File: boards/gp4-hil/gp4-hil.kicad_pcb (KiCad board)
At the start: 4 copper layers, 160 x 62 mm, 452 parts, among them J1 BEL_FUSE_0826-1G1T-23-F, J2 XILINX_JTAG, J3 XILINX_JTAG_ICESIDE, J4 XILINX_JTAG_ICESIDE, K1 CONN_3_PWROUT, P1 GPAK_ZIF, P2 2x10 HEADER, Q1 SSM6N58NU, Q11 SSM6N58NU, Q12 DMP2069UFY4, Q13 SSM6N58NU, Q14 SSM6N58NU, Q15 SSM6N58NU, Q16 SSM6N58NU, Q17 SSM6N58NU, Q18 SSM6N58NU, Q19 SSM6N58NU, Q20 SSM6N58NU, Q21 SSM6N58NU, Q22 DMP2069UFY4, U1 MIC2288-DFN, U10 AD9609, U11 DAC084S085, U12 DAC084S085, U13 DAC084S085, U14 DAC084S085, U15 TS3A4751, U16 TS3A4751, U17 TS3A4751, U18 TS3A4751, U19 TS3A4751, U2 XC7A100T-1FTG256C, U20 SIP32408, U21 SIP32408, U22 SIP32408, U23 SIP32408, U24 SIP32408, U25 TS3A4751, U26 TS3A4751, U27 TS3A4751, U28 TS3A4751, U29 TXB0104RUT, U3 LTC3374-QFN, U30 TXB0104RUT, U31 ADA4937-2, U32 SIP32408, U33 125 MHz, U34 INA199A2RSW, U35 INA199A2RSW, U36 INA199A2RSW, U4 SIP32408, U5 KSZ9031RN, U6 W25Q32FW, U7 25 MHz, U8 ADG726, U9 AD9609

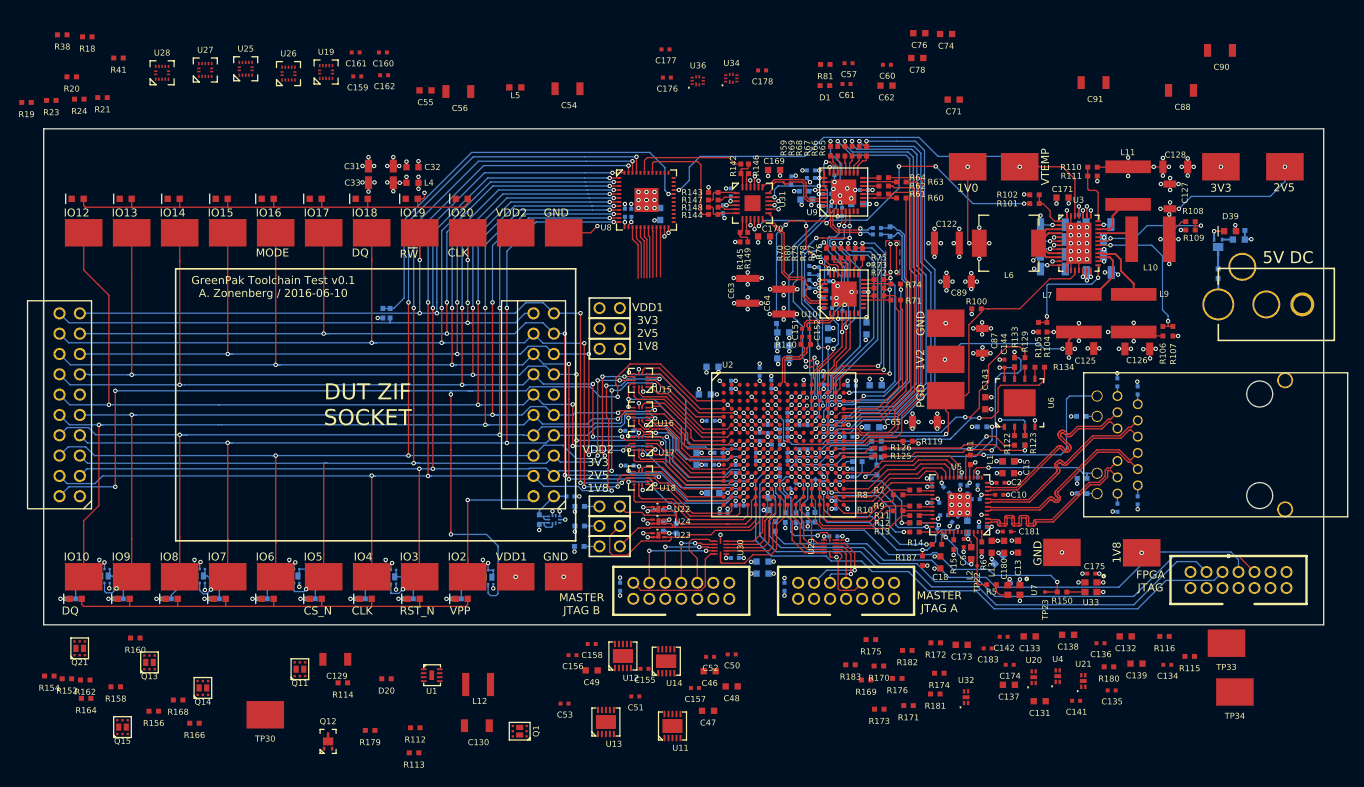
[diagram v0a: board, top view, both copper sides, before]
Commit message: Continued work on dev board layout. Hooked up analog mux.
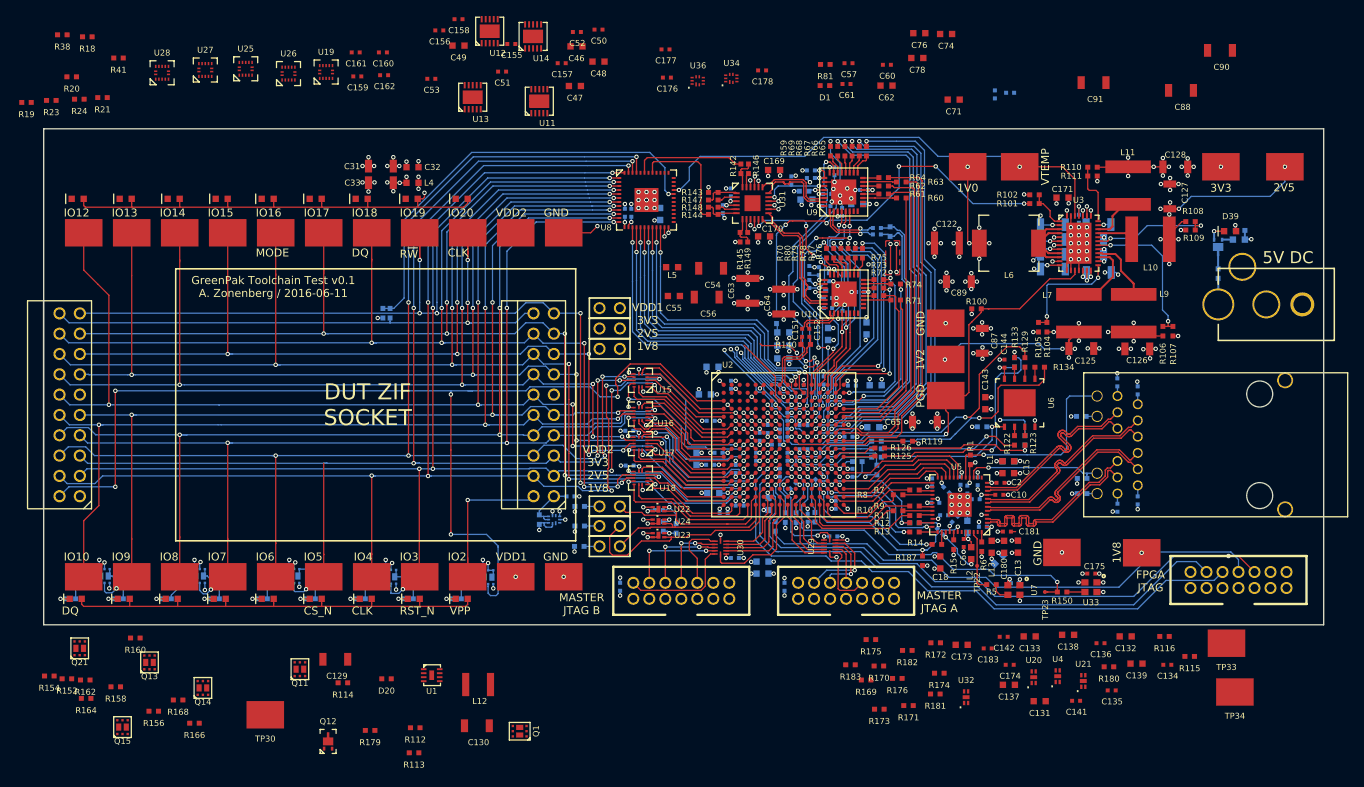
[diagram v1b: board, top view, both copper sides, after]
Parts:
- moved C157 79.9 mm to (85.8, 49.8)
- moved C158 79.9 mm to (72.8, 44.3)
- moved U11 79.9 mm to (83.0, 54.5)
- moved U12 79.9 mm to (76.8, 45.8)
- moved U13 79.9 mm to (74.6, 54.0)
- moved C155 79.9 mm to (79.5, 47.4)
- moved C156 79.9 mm to (70.5, 45.7)
- moved C46 79.9 mm to (87.6, 47.7)
- moved C47 79.9 mm to (87.4, 52.6)
- moved C48 79.9 mm to (90.3, 49.6)
- moved C49 79.9 mm to (72.8, 47.6)
- moved C50 79.9 mm to (90.3, 45.6)
- moved C51 79.9 mm to (78.3, 50.9)
- moved C52 79.9 mm to (87.7, 45.9)
- moved C53 79.9 mm to (69.5, 51.8)
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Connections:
- U2 pad A10: /Analog IO/MUX_WR_N -> /Analog IO/MUX_CS_B_N
- U2 pad B10: /Analog IO/MUX_EN_N -> /Analog IO/MUX_CS_A_N
- U2 pad B11: /Analog IO/MUX_A3 -> /Analog IO/MUX_WR_N
- U2 pad B9: /Analog IO/MUX_CS_B_N -> /Analog IO/MUX_A1
- U2 pad C11: /Analog IO/DAC_SYNC_N -> /Analog IO/MUX_EN_N
- U2 pad C8: /Analog IO/MUX_A1 -> /Analog IO/DAC_B_DIN
- U2 pad C9: /Analog IO/MUX_A2 -> /Analog IO/MUX_A0
- U2 pad D10: /Analog IO/MUX_A0 -> /Analog IO/MUX_A2
- U2 pad D11: /Analog IO/DAC_B_DIN -> /Analog IO/MUX_A3
- U2 pad G11: /Analog IO/MUX_CS_A_N -> /Analog IO/DAC_SYNC_N
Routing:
- net /Analog IO/MUX_A3: track 6.47 -> 39.7 mm, vias 0 -> 2
- net /Analog IO/MUX_EN_N: track 6.20 -> 37.8 mm, vias 0 -> 2
- net /Analog IO/MUX_A2: track 7.24 -> 38.8 mm, vias 1 -> 2
- net /Analog IO/MUX_A0: track 7.40 -> 38.0 mm, vias 1 -> 2
- net /Analog IO/MUX_WR_N: track 6.20 -> 36.5 mm, vias 0 -> 2
- net /Analog IO/MUX_CS_A_N: track 6.36 -> 35.9 mm, vias 0 -> 2
- net /Analog IO/MUX_A1: track 7.26 -> 35.9 mm, vias 1 -> 2
- net /Analog IO/MUX_CS_B_N: track 6.32 -> 35.0 mm, vias 0 -> 2
- net /Analog IO/DAC_SYNC_N: track 0.57 -> 17.9 mm, vias 1 -> 2
- net /Analog IO/DAC_A_DIN: track 0.71 -> 14.3 mm, vias 1 -> 2
- net /Analog IO/DAC_C_DIN: track 0.71 -> 10.2 mm, vias 1 -> 2
- net /Analog IO/DAC_SCLK: track 0.71 -> 9.98 mm, vias 1 -> 2
- net /Analog IO/DAC_B_DIN: track 0.57 -> 8.79 mm, vias 1 -> 0
- net /Analog IO/DAC_D_DIN: track 9.99 -> 17.3 mm, vias 3 -> 4
- net /Analog IO/DUT_VDD1: track 150.9 -> 149.1 mm
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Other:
- board text added: "GreenPak Toolchain Test v0.1 A. Zonenberg / 2016-06-11"
- board text removed: "GreenPak Toolchain Test v0.1 A. Zonenberg / 2016-06-10"

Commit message: Continued layout, down to 288 unrouted nets. Working mostly on ADC inputs plus bus re-routing.
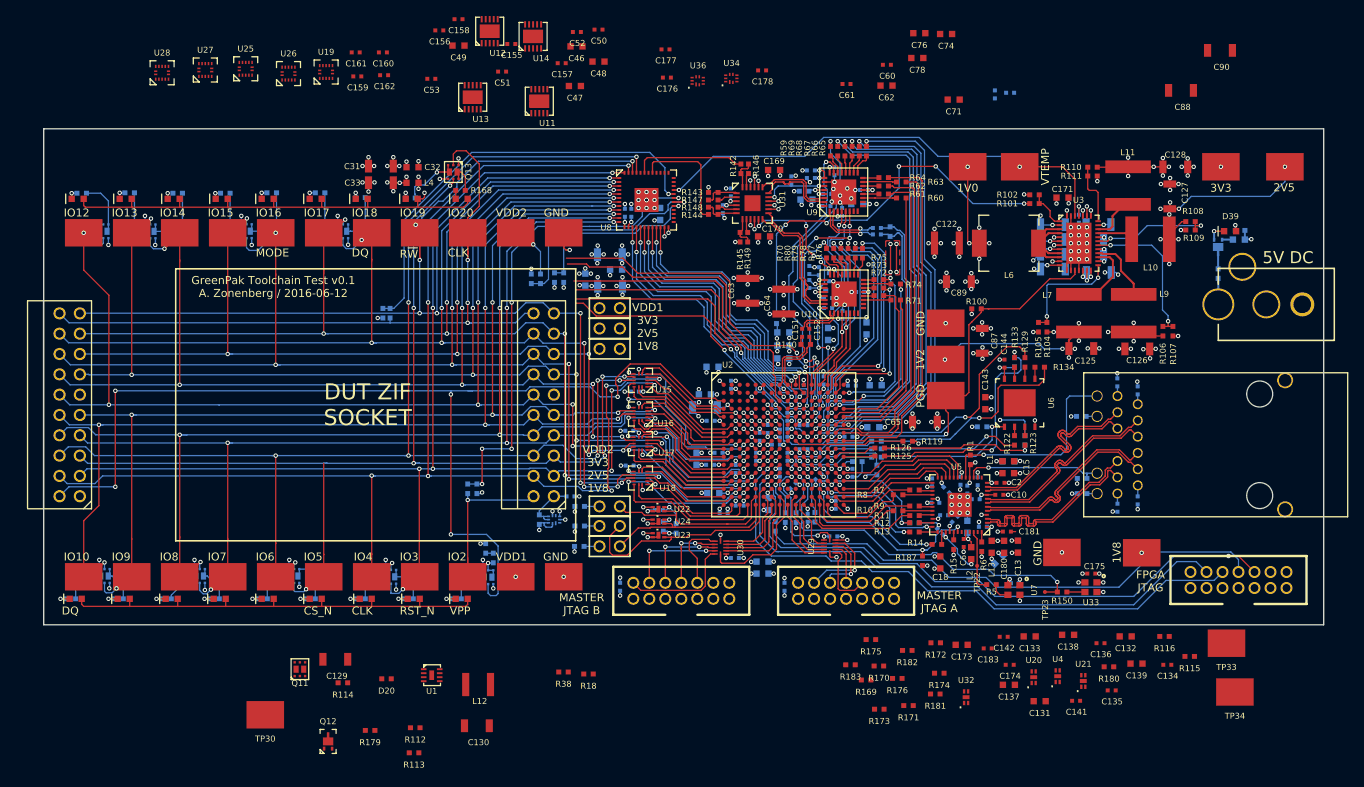
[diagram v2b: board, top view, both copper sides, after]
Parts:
- C54, C55, C56, C57, C91, D1, L5, Q1, Q14, Q15, Q21, R152, R154, R156, R158, R160, R162, R164, R166, R19, R20, R21, R23, R24, R41, R81: moved to B.Cu
- moved R18 101.3 mm to (89.1, 126.2)
- moved R38 101.3 mm to (86.0, 125.9)
- moved Q1 81.3 mm to (28.4, 70.8), turned to 180 degrees
- moved R81 74.4 mm to (77.2, 111.7), turned to 270 degrees
- moved R168 72.8 mm to (73.1, 65.7), turned to 180 degrees
- moved Q13 72.1 mm to (72.2, 63.4), turned to 180 degrees
- moved D1 71.7 mm to (76.2, 110.5), turned to 90 degrees
- moved R20 71.4 mm to (74.0, 103.0), turned to 270 degrees
- moved R164 71.4 mm to (60.6, 66.6), turned to 180 degrees
- moved R166 71.0 mm to (66.8, 66.7), turned to 180 degrees
- moved R41 70.0 mm to (75.2, 103.0), turned to 90 degrees
- moved R19 69.5 mm to (84.8, 76.6), turned to 270 degrees
- moved R23 67.8 mm to (86.0, 76.6), turned to 90 degrees
- moved R162 67.6 mm to (55.5, 66.0), turned to 180 degrees
- moved R156 64.8 mm to (37.7, 66.0), turned to 180 degrees
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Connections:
- Q1 pad G1: /Analog IO/DUT_GPIO18 -> /Analog IO/DUT_GPIO12
- Q11 pad D2: Net-(Q11-PadD2) -> (no net)
- Q11 pad G2: /Analog IO/DUT_GPIO19 -> (no net)
- Q11 pad S2: /Analog IO/GND -> (no net)
- Q13 pad G1: /Analog IO/DUT_GPIO15 -> /Analog IO/DUT_GPIO20
- Q13 pad G2: /Analog IO/DUT_GPIO12 -> /Analog IO/DUT_GPIO19
- Q14 pad G1: /Analog IO/DUT_GPIO16 -> /Analog IO/DUT_GPIO18
- Q14 pad G2: /Analog IO/DUT_GPIO13 -> /Analog IO/DUT_GPIO17
- Q15 pad G1: /Analog IO/DUT_GPIO17 -> /Analog IO/DUT_GPIO16
- Q15 pad G2: /Analog IO/DUT_GPIO14 -> /Analog IO/DUT_GPIO15
- Q21 pad D2: (no net) -> Net-(Q21-PadD2)
- Q21 pad G1: /Analog IO/DUT_GPIO20 -> /Analog IO/DUT_GPIO14
- Q21 pad G2: (no net) -> /Analog IO/DUT_GPIO13
- Q21 pad S2: (no net) -> /Analog IO/GND
- R152 pad 1: Net-(Q13-PadD2) -> Net-(Q1-PadD1)
- R154 pad 1: Net-(Q14-PadD2) -> Net-(Q21-PadD2)
- R156 pad 1: Net-(Q15-PadD2) -> Net-(Q21-PadD1)
- R158 pad 1: Net-(Q13-PadD1) -> Net-(Q15-PadD2)
- R160 pad 1: Net-(Q14-PadD1) -> Net-(Q15-PadD1)
- R162 pad 1: Net-(Q15-PadD1) -> Net-(Q14-PadD2)
- R164 pad 1: Net-(Q1-PadD1) -> Net-(Q14-PadD1)
- R166 pad 1: Net-(Q11-PadD2) -> Net-(Q13-PadD2)
- R168 pad 1: Net-(Q21-PadD1) -> Net-(Q13-PadD1)
- U8 pad 29: /Analog IO/ADC_GPIO2 -> /Analog IO/ADC_VDD1
- U8 pad 31: /Analog IO/ADC_VDD1 -> /Analog IO/ADC_GPIO2
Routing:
- net /Analog IO/GND: track 1236.3 -> 1353.0 mm, vias 242 -> 267
- net /Analog IO/ADC_GPIO2: track 0.00 -> 60.2 mm, vias 0 -> 5
- net /Analog IO/DUT_VDD1: track 149.1 -> 184.5 mm, vias 16 -> 20
- net /Analog IO/DAC_D_DIN: track 17.3 -> 48.9 mm
- net /Analog IO/DAC_B_DIN: track 8.79 -> 39.8 mm
- net /Analog IO/DAC_C_DIN: track 10.2 -> 38.2 mm
- net /Analog IO/ADC_VDD2: track 0.00 -> 27.5 mm, vias 0 -> 1
- net /Analog IO/DAC_A_DIN: track 14.3 -> 39.9 mm
- net /Analog IO/DAC_SCLK: track 9.98 -> 33.9 mm
- net /Analog IO/ADC_VDD1: track 0.00 -> 22.3 mm, vias 0 -> 1
- net /Analog IO/DAC_SYNC_N: track 17.9 -> 39.8 mm
- net /Analog IO/DUT_GPIO20: track 76.3 -> 91.0 mm
- net /Analog IO/3V3: track 239.8 -> 253.5 mm, vias 9 -> 15
- net /Analog IO/A3V3: track 49.9 -> 61.3 mm, vias 12 -> 16
- net /Analog IO/DUT_GPIO19: track 142.0 -> 150.9 mm, vias 7 -> 9
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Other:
- board text added: "GreenPak Toolchain Test v0.1 A. Zonenberg / 2016-06-12"
- board text removed: "ADCs"
- board text removed: "DUT indicator LEDs"
- board text removed: "GreenPak Toolchain Test v0.1 A. Zonenberg / 2016-06-11"

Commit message: Continued routing of DUT load switches, ADC inputs, etc. 228 unrouted.
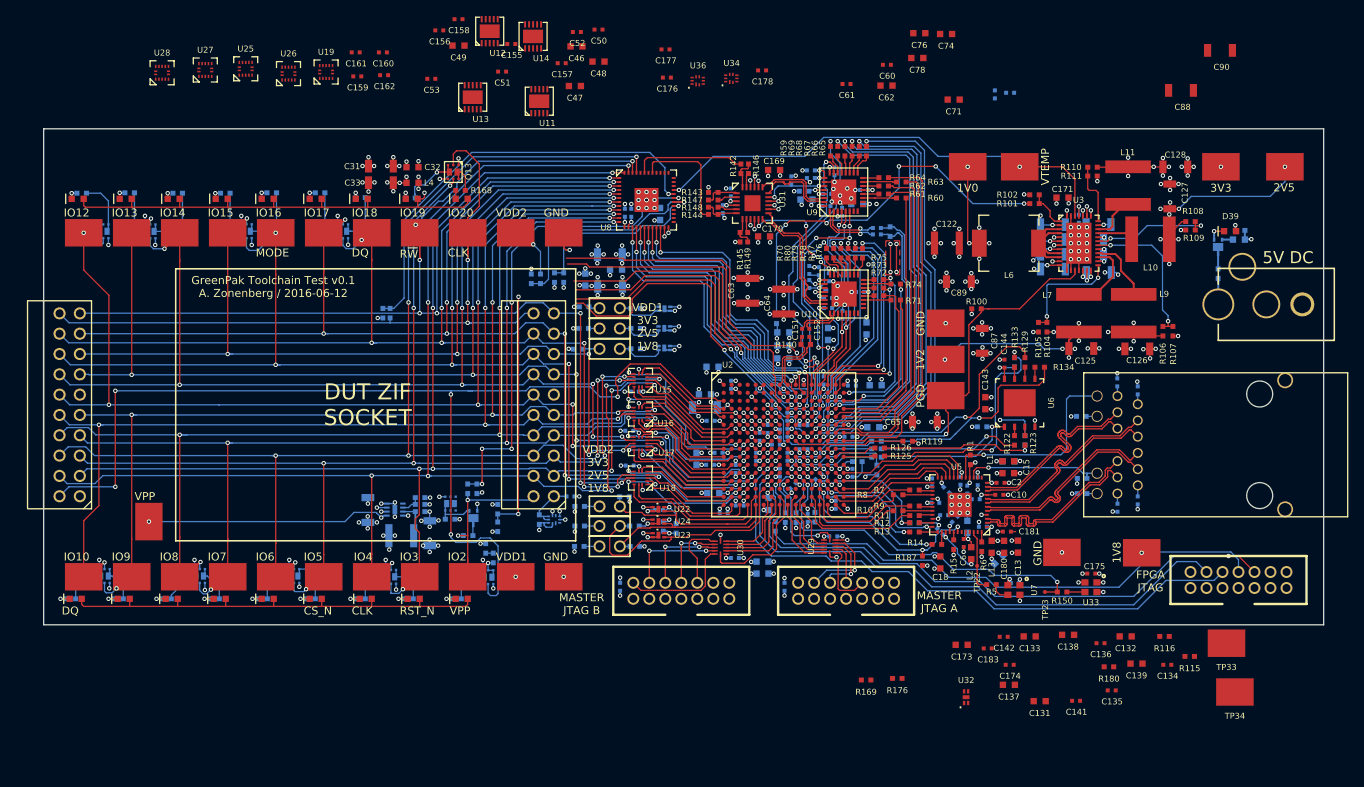
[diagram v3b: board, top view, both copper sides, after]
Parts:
- C129, C130, D20, L12, Q11, Q12, R112, R113, R114, R170, R171, R172, R173, R174, R175, R179, R18, R181, R182, R183, R38, U1, U20, U21, U4: moved to B.Cu
- moved U4 67.3 mm to (98.6, 80.5), turned to 270 degrees
- moved U21 66.9 mm to (98.6, 85.4), turned to 270 degrees
- moved R181 65.3 mm to (88.5, 80.2)
- moved U20 63.5 mm to (98.6, 83.0), turned to 270 degrees
- moved R171 58.2 mm to (95.0, 83.0), turned to 180 degrees
- moved R182 57.1 mm to (88.5, 83.0)
- moved R170 54.1 mm to (95.0, 80.5), turned to 180 degrees
- moved R172 52.5 mm to (95.0, 85.5), turned to 180 degrees
- moved R183 52.1 mm to (87.8, 85.5)
- moved R174 42.3 mm to (94.8, 107.7), turned to 180 degrees
- moved R173 41.5 mm to (93.6, 104.0), turned to 180 degrees
- moved Q12 33.3 mm to (74.7, 106.7)
- moved R113 31.9 mm to (68.0, 104.1)
- moved R175 31.7 mm to (94.9, 110.2), turned to 180 degrees
- moved TP30 28.2 mm to (34.1, 107.1), turned to 90 degrees
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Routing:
- net /Analog IO/GND: track 1353.0 -> 1412.2 mm, vias 267 -> 287
- net /Analog IO/DUT_VPP: track 0.00 -> 57.0 mm, vias 0 -> 10
- net /Analog IO/ADC_VPP: track 0.00 -> 30.7 mm, vias 0 -> 2
- net /Analog IO/1V8: track 483.0 -> 505.8 mm, vias 60 -> 64
- net /Power supply/5V0: track 92.0 -> 111.1 mm, vias 24 -> 33
- net /Analog IO/3V3: track 253.5 -> 266.8 mm, vias 15 -> 16
- net /Analog IO/DAC_SYNC_N: track 39.8 -> 46.8 mm
- net /Ethernet + JTAG/VDD1_1V8_EN: track 0.71 -> 6.76 mm
- net /Ethernet + JTAG/VDD1_2V5_EN: track 0.00 -> 5.91 mm
- net /Ethernet + JTAG/VDD1_3V3_EN: track 0.71 -> 6.57 mm
- net /Power supply/VPP_EN_HV_N: track 0.00 -> 5.23 mm
- net /Analog IO/DUT_VDD1: track 184.5 -> 189.5 mm
- net Net-(D20-Pad2): track 0.00 -> 4.65 mm
- net /Analog IO/DAC_SCLK: track 33.9 -> 37.5 mm
- net /Analog IO/DAC_A_DIN: track 39.9 -> 42.7 mm
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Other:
- board text removed: "Vpp supply"
